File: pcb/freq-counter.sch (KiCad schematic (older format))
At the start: 64 parts, among them J1 RPM on board, J10 Power_T1, J11 Hz/RPM_Terminal1, J12 Hz/RPM_Terminal0, J13 1kMG_Terminal1, J14 1kMG_Terminal0, J2 BNC, J3 RPM to Board, J4 Jack-DC, J5 Segments-Terminal0, J6 Digits-Terminal0, J7 Segments-Terminal1, J8 Digits-Terminal1, J9 Power_Terminal1, Q1 CSC388A, Q2 CSC388A, Q3 2SA1015, Q4 2SC1815, Q5 2SC1815, SW1 on/off, SW2 count up, SW3 toggle, SW4 SW_SIGNAL, U1 SN74HC02N, U2 ATTINY4313-PU(freq-counter), U3 EE-SX460, Y1 10MHz

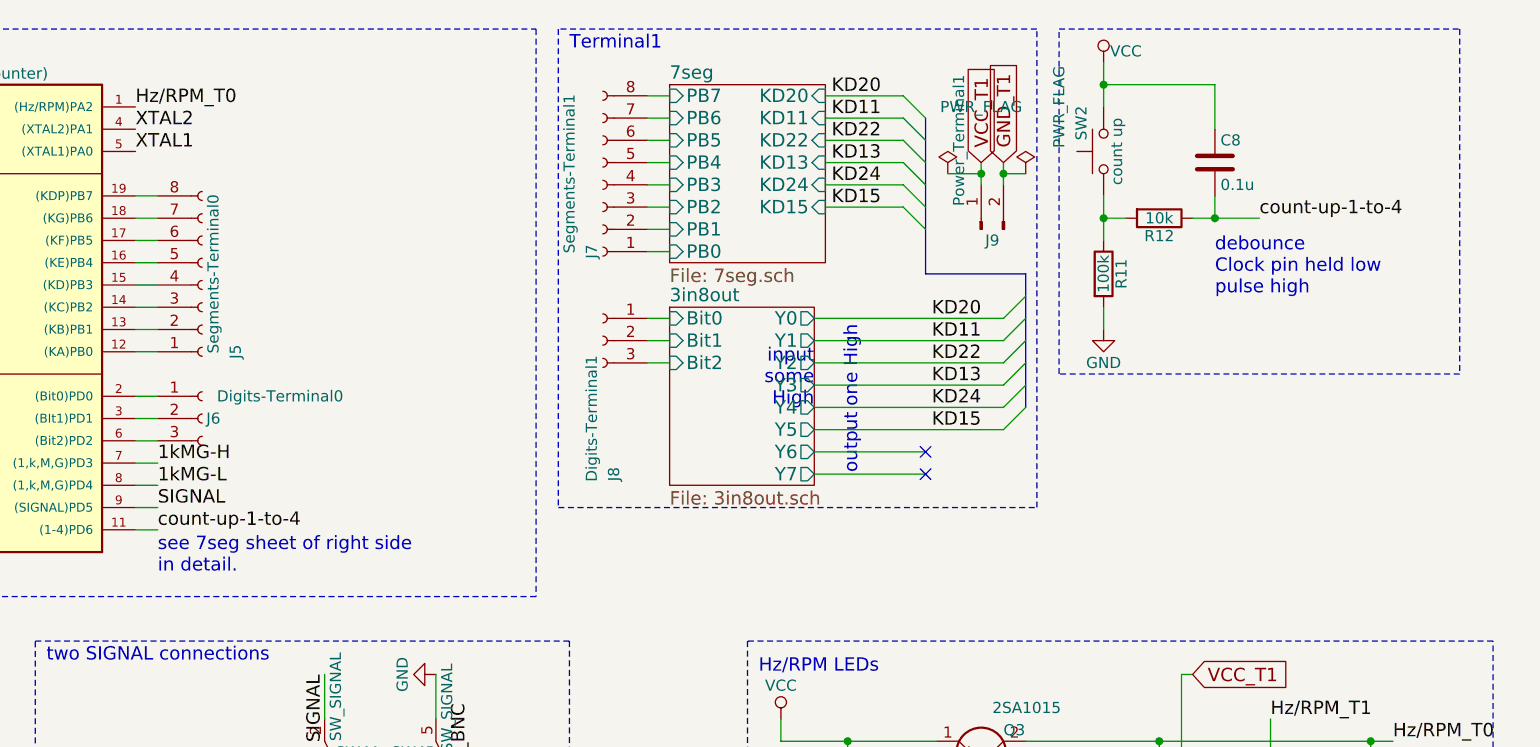
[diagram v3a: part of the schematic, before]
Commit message: count-up を Terminal 化した。
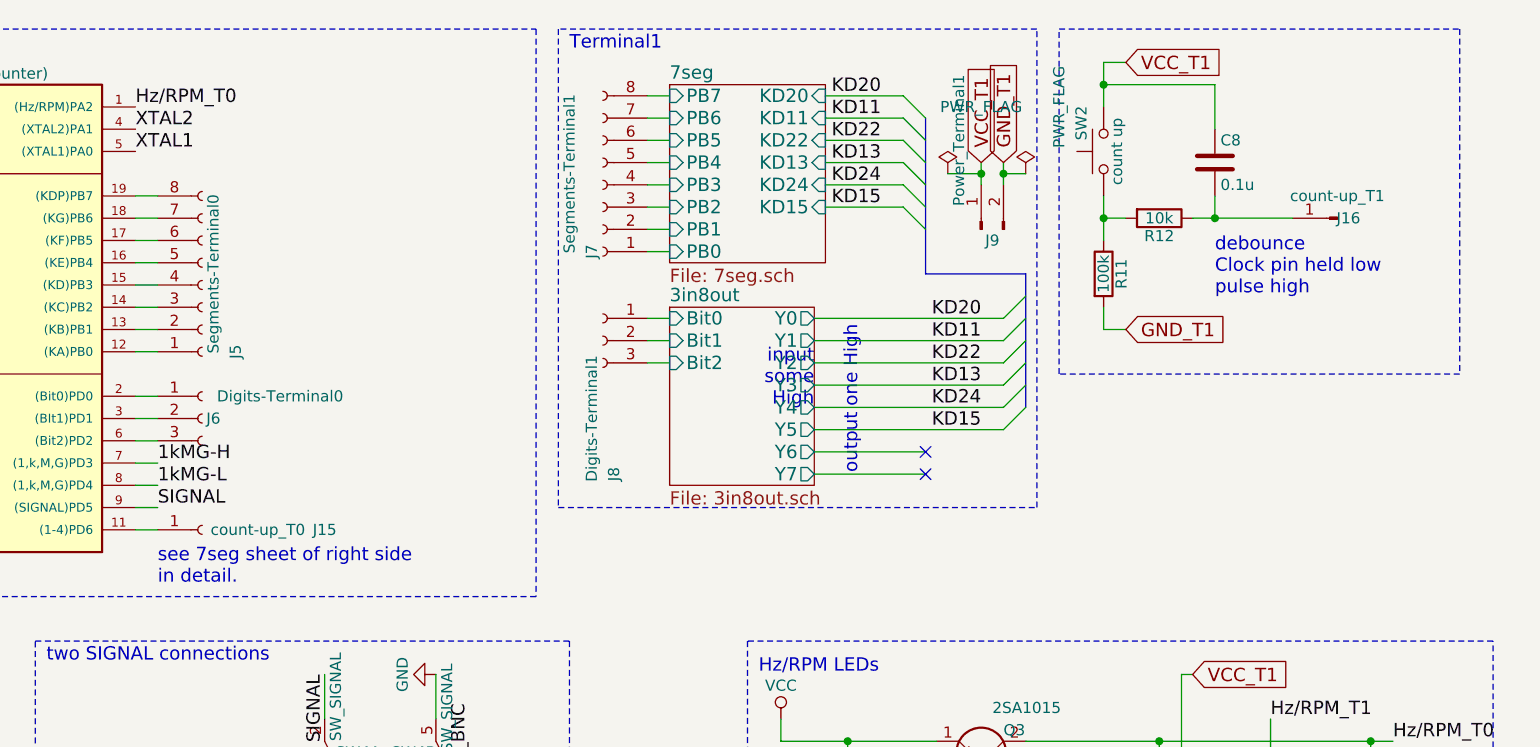
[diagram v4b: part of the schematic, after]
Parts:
- added J15: count-up_T0, Connector_PinSocket_2.54mm:PinSocket_1x01_P2.54mm_Vertical, symbol Conn_01x01_Female
- added J16: count-up_T1, Connector_PinHeader_2.54mm:PinHeader_1x01_P2.54mm_Vertical, symbol Conn_01x01_Male
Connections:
- net GND: no longer R11.2
- net GND_T1: now also R11.2
- net VCC: no longer C8.1, SW2.2
- net VCC_T1: now also C8.1, SW2.2
- net count-up-1-to-4: no longer names the net of C8.2, R12.1
- net count-up-1-to-4: now also J16.1 (Pin_1); no longer U2.11 ((1-4)PD6)
- new net: J15.1 (Pin_1), U2.11 ((1-4)PD6)
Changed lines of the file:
@@
 	1    0    0    -1
 $EndComp
-Text Label 10050 1600 0    60   ~ 0
-count-up-1-to-4
 $Comp
 L 2SC1815 Q5
@@
 Entry Wire Line
 	8900 2450 9000 2350
-Text Label 5100 3000 0    60   ~ 0
-count-up-1-to-4
-Text Notes 5100 3200 0    60   ~ 0
+Text Notes 5100 3250 0    60   ~ 0
 see 7seg sheet of right side\nin detail.
 Text Notes 3100 850  0    60   ~ 0
@@
 	9850 1600 9850 1500
 Wire Wire Line
-	9750 1600 10050 1600
+	9750 1600 10200 1600
 Connection ~ 9350 1600
 Wire Wire Line
@@
 	7900 3950 7900 3850
 $Comp
-L VCC #PWR022
-U 1 1 5A1F1808
-P 9350 900
-F 0 "#PWR022" H 9350 750 50  0001 C CNN
-F 1 "VCC" H 9450 950 50  0000 C CNN
-F 2 "" H 9350 900 50  0001 C CNN
-F 3 "" H 9350 900 50  0001 C CNN
-	1    9350 900
-	1    0    0    -1
-$EndComp
-$Comp
-L GND #PWR023
-U 1 1 5A1F21A6
-P 9350 2100
-F 0 "#PWR023" H 9350 1850 50  0001 C CNN
-F 1 "GND" H 9350 1950 50  0000 C CNN
-F 2 "" H 9350 2100 50  0001 C CNN
-F 3 "" H 9350 2100 50  0001 C CNN
-	1    9350 2100
-	1    0    0    -1
-$EndComp
-$Comp
-L GND #PWR024
+L GND #PWR022
 U 1 1 5A1F3CDE
 P 6350 3650
-F 0 "#PWR024" H 6350 3400 50  0001 C CNN
+F 0 "#PWR022" H 6350 3400 50  0001 C CNN
 F 1 "GND" H 6350 3500 50  0000 C CNN
 F 2 "" H 6350 3650 50  0001 C CNN
@@
 $EndComp
 $Comp
-L VCC #PWR025
+L VCC #PWR023
 U 1 1 5A1F4C25
 P 5800 4400
-F 0 "#PWR025" H 5800 4250 50  0001 C CNN
+F 0 "#PWR023" H 5800 4250 50  0001 C CNN
 F 1 "VCC" H 5800 4550 50  0000 C CNN
 F 2 "" H 5800 4400 50  0001 C CNN
@@
 Text Label 900  4300 0    60   ~ 0
 LED_G
+Text GLabel 9450 900  2    60   Input ~ 0
+VCC_T1
+Wire Wire Line
+	9350 900  9450 900
+Text GLabel 9450 2100 2    60   Input ~ 0
+GND_T1
+Wire Wire Line
+	9350 2100 9450 2100
+$Comp
+L Conn_01x01_Male J16
+U 1 1 5A20B3ED
+P 10400 1600
+F 0 "J16" H 10350 1600 50  0000 C CNN
+F 1 "count-up_T1" H 10400 1500 50  0000 C CNN
+F 2 "Connector_PinHeader_2.54mm:PinHeader_1x01_P2.54mm_Vertical" H 10400 1600 50  0001 C CNN
+F 3 "" H 10400 1600 50  0001 C CNN
+	1    10400 1600
+	-1   0    0    1
+$EndComp
+$Comp
+L Conn_01x01_Female J15
+U 1 1 5A20DDD4
+P 5300 3000
+F 0 "J15" H 5850 3000 50  0000 C CNN
+F 1 "count-up_T0" H 5550 3000 50  0000 C CNN
+F 2 "Connector_PinSocket_2.54mm:PinSocket_1x01_P2.54mm_Vertical" H 5300 3000 50  0001 C CNN
+F 3 "" H 5300 3000 50  0001 C CNN
+	1    5300 3000
+	1    0    0    -1
+$EndComp
 $EndSCHEMATC

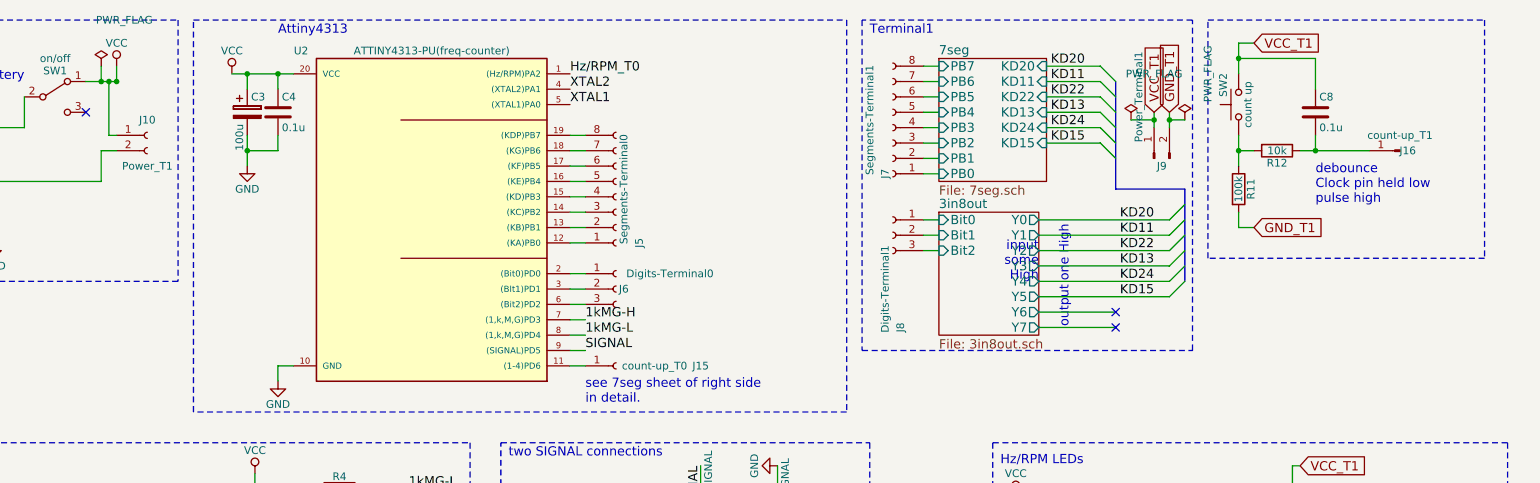
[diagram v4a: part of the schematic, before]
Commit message: combine Segments-Terminal? and count-up-Terminal?
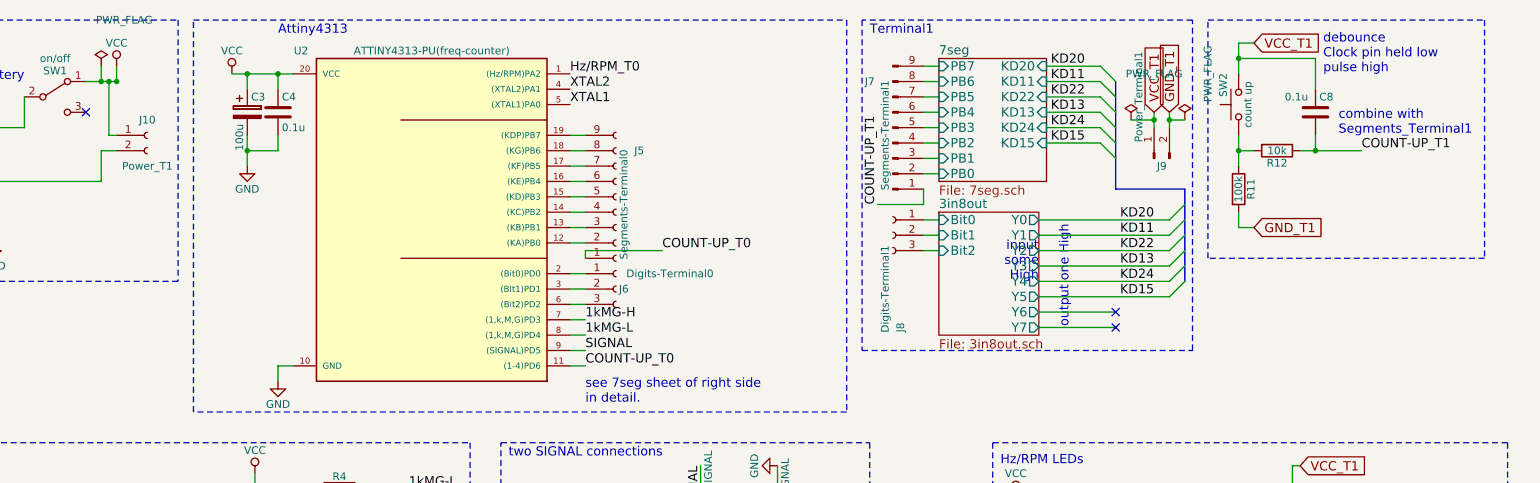
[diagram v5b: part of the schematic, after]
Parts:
- removed J15: count-up_T0, Connector_PinSocket_2.54mm:PinSocket_1x01_P2.54mm_Vertical, symbol Conn_01x01_Female
- removed J16: count-up_T1, Connector_PinHeader_2.54mm:PinHeader_1x01_P2.54mm_Vertical, symbol Conn_01x01_Male
- removed J5: Segments-Terminal0, Connector_PinSocket_2.54mm:PinSocket_1x08_P2.54mm_Vertical, symbol Conn_01x08_Female
- removed J7: Segments-Terminal1, Connector_PinHeader_2.54mm:PinHeader_1x08_P2.54mm_Vertical, symbol Conn_01x08_Female
- added J5: Segments-Terminal0, Connector_PinSocket_2.54mm:PinSocket_1x09_P2.54mm_Vertical, symbol Conn_01x09_Female
- added J7: Segments-Terminal1, Connector_PinHeader_2.54mm:PinHeader_1x09_P2.54mm_Vertical, symbol Conn_01x09_Male
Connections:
- net 7seg/PB0: now also J7.2 (Pin_2)
- net 7seg/PB1: now also J7.3 (Pin_3)
- net 7seg/PB2: now also J7.4 (Pin_4)
- net 7seg/PB3: now also J7.5 (Pin_5)
- net 7seg/PB4: now also J7.6 (Pin_6)
- net 7seg/PB5: now also J7.7 (Pin_7)
- net 7seg/PB6: now also J7.8 (Pin_8)
- net 7seg/PB7: now also J7.9 (Pin_9)
- net COUNT-UP_T1: now reaches C8.2, R12.1
- net COUNT-UP_T1: now also J7.1 (Pin_1)
- net COUNT-UP_T0: now reaches U2.11 ((1-4)PD6)
- net COUNT-UP_T0: now also J5.1 (Pin_1)
- net at U2.12 ((KA)PB0): now also J5.2 (Pin_2)
- net at U2.13 ((KB)PB1): now also J5.3 (Pin_3)
- net at U2.14 ((KC)PB2): now also J5.4 (Pin_4)
- net at U2.15 ((KD)PB3): now also J5.5 (Pin_5)
- net at U2.16 ((KE)PB4): now also J5.6 (Pin_6)
- net at U2.17 ((KF)PB5): now also J5.7 (Pin_7)
- net at U2.18 ((KG)PB6): now also J5.8 (Pin_8)
- net at U2.19 ((KDP)PB7): now also J5.9 (Pin_9)
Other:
- note added: "combine with\nSegments_Terminal1"

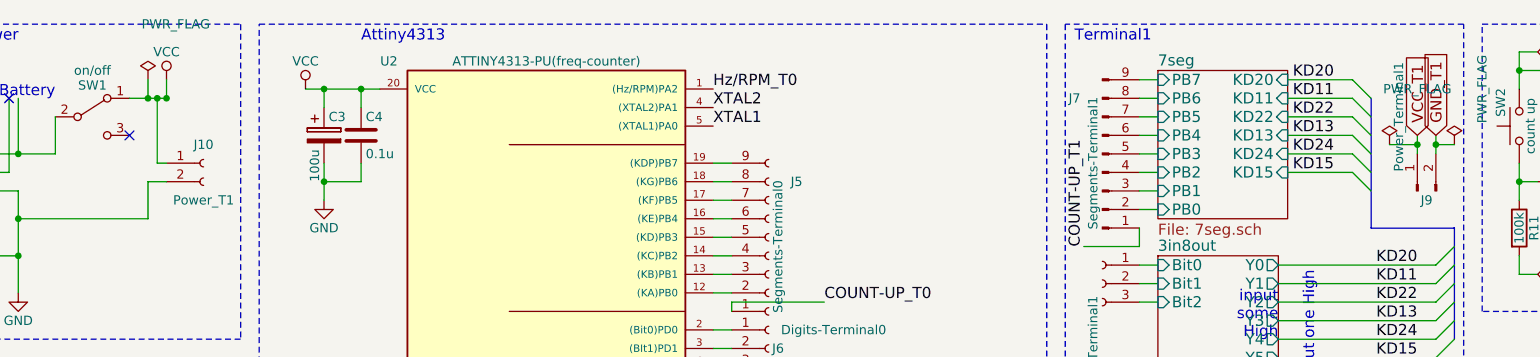
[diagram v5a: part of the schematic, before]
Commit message: Terminal0 系を配置。
後は上手く配線をするだけ。
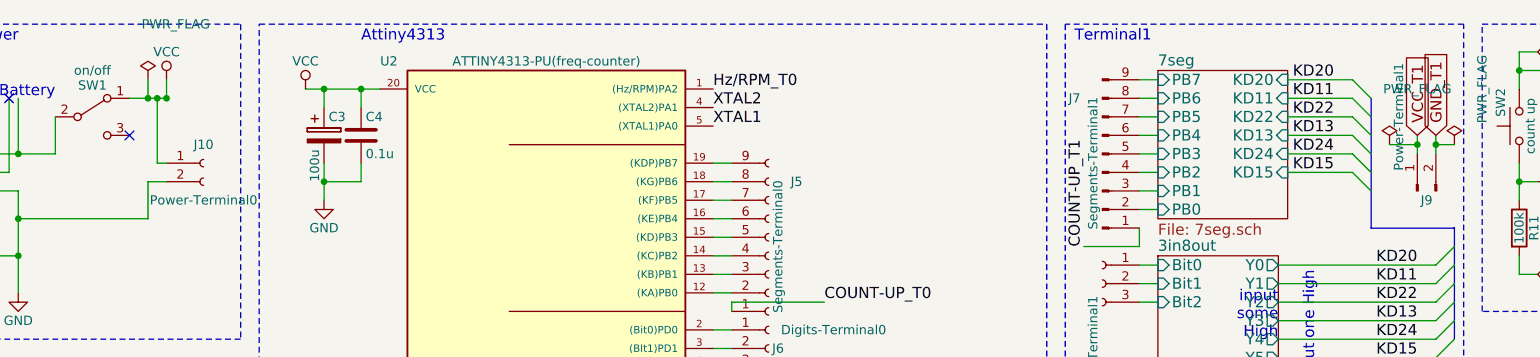
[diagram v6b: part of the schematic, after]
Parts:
- J10: value Power_T1 -> Power-Terminal0
- J9: value Power_Terminal1 -> Power-Terminal1
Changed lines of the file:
@@
 P 8800 1650
 F 0 "J9" V 8750 1600 50  0000 C CNN
-F 1 "Power_Terminal1" H 9200 1750 50  0000 C CNN
+F 1 "Power-Terminal1" H 9200 1750 50  0000 C CNN
 F 2 "Conn_JST:JST_XH_B02B-XH-A_1x02_P2.50mm_Horizontal" H 8800 1650 50  0001 C CNN
 F 3 "" H 8800 1650 50  0001 C CNN
@@
 P 2250 1500
 F 0 "J10" H 2250 1600 50  0000 C CNN
-F 1 "Power_T1" H 2250 1300 50  0000 C CNN
+F 1 "Power-Terminal0" H 2250 1300 50  0000 C CNN
 F 2 "Conn_JST:JST_XH_B02B-XH-A_1x02_P2.50mm_Horizontal" H 2250 1500 50  0001 C CNN
 F 3 "" H 2250 1500 50  0001 C CNN
@@
 	2050 1500 2000 1500
 Wire Wire Line
-	2000 1150 2000 1500
+	2000 1500 2000 1150
 Connection ~ 2000 1150
 Wire Wire Line

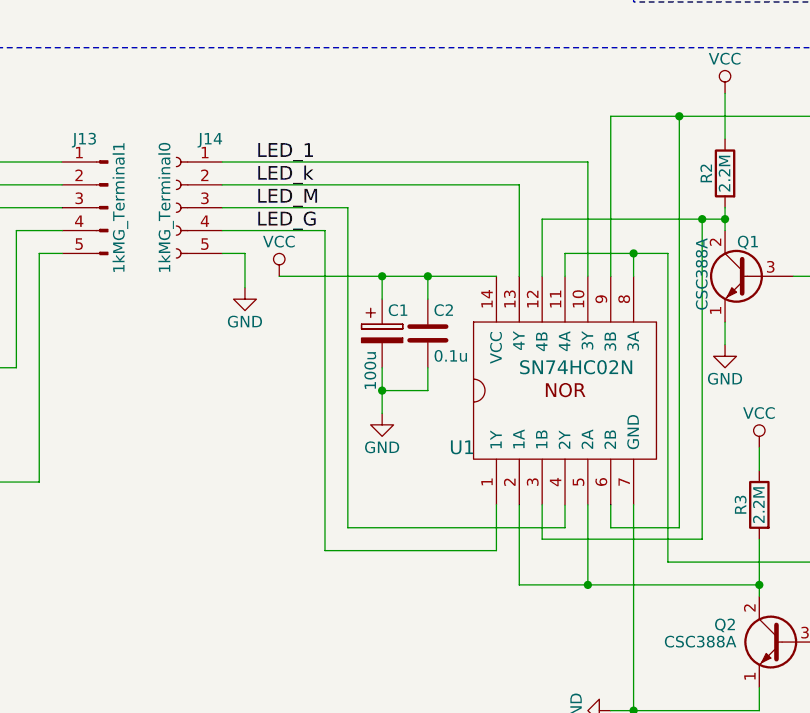
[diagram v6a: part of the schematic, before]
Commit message: SN74HC02N(U1)の，LED_1 <-> LED_k, LED_M <-> LED-G の配線をそれぞれ入れ替えた。
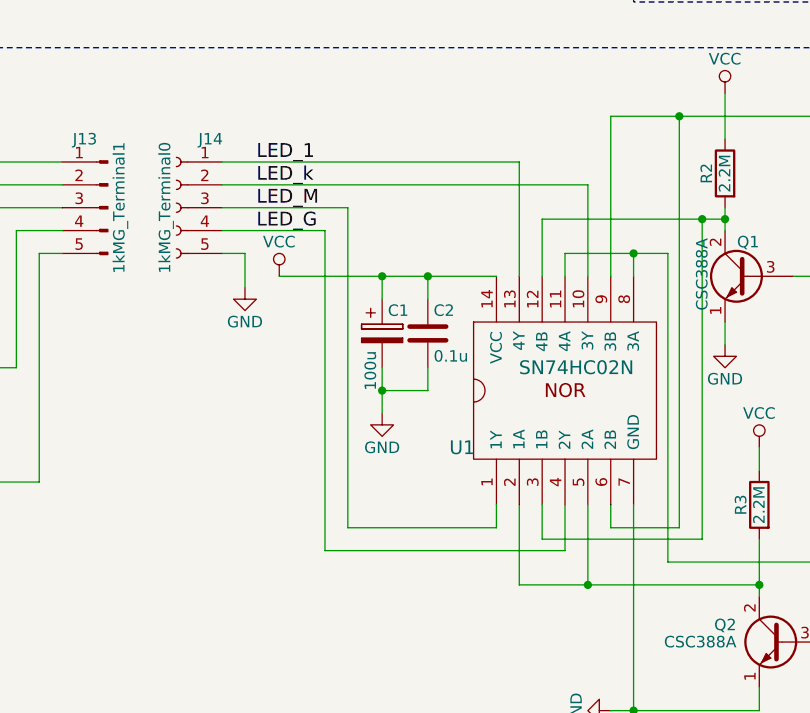
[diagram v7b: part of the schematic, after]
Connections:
- net LED_1: now also U1.13 (4Y); no longer U1.10 (3Y)
- net LED_G: now also U1.4 (2Y); no longer U1.1 (1Y)
- net LED_M: now also U1.1 (1Y); no longer U1.4 (2Y)
- net LED_k: now also U1.10 (3Y); no longer U1.13 (4Y)
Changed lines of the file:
@@
 	-350 4300 -600 4300
 Wire Wire Line
-	2050 4100 2050 4500
-Wire Wire Line
 	-600 4000 50   4000
-Wire Wire Line
-	2350 4000 2350 4500
 Wire Wire Line
 	1000 4500 1950 4500
@@
 	3100 5650 3100 5900
 Wire Wire Line
-	2250 5500 2250 5600
-Wire Wire Line
 	-250 4600 -600 4600
-Wire Wire Line
-	1950 5500 1950 5700
 Wire Wire Line
 	-600 4900 -150 4900
@@
 	-50  5400 -1050 5400
 Wire Wire Line
-	750  4000 2350 4000
-Wire Wire Line
-	750  4100 2050 4100
+	750  4100 2350 4100
 Wire Wire Line
 	750  4300 1200 4300
@@
 	1200 4300 1200 5700
 Wire Wire Line
-	1200 5700 1950 5700
+	1200 5700 2250 5700
 Wire Wire Line
 	750  4200 1300 4200
 Wire Wire Line
 	1300 4200 1300 5600
-Wire Wire Line
-	1300 5600 2250 5600
 Wire Wire Line
 	750  4400 850  4400
@@
 Wire Wire Line
 	5100 2300 5100 2250
+Wire Wire Line
+	2350 4100 2350 4500
+Wire Wire Line
+	750  4000 2050 4000
+Wire Wire Line
+	2050 4000 2050 4500
+Wire Wire Line
+	1300 5600 1950 5600
+Wire Wire Line
+	1950 5600 1950 5500
+Wire Wire Line
+	2250 5700 2250 5500
 $EndSCHEMATC
